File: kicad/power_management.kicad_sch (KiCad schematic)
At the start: 30 parts, among them J17 PJ-002AH, SW1 RESET, U1 TPS54302DDCR, U12 TPS3823-33DBVR, U2 AMS1117-3.3

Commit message: fix: Embed lib_symbols, fix invalid lib_ids, bump to KiCad 9 format
- Embed complete (lib_symbols) definitions in all 5 sub-sheets so symbols
  render as real parts instead of '??' placeholders (files now self-contained)
- Substitute invalid lib_ids with valid library symbols:
  Device:CP -> Device:C_Polarized, Diode:PESD3V3S2USF -> Diode:PESD3V3S1UL,
  Diode:PESD5V0S1BSF -> Diode:PESD5V0S1UL, Isolator:PC817X2 -> Isolator:PC817
- Bump file format version 20231120 -> 20250114 (removes 'older version' warning)
- Left-justify header text blocks so long lines stay within the A3 frame

Validated: kicad-cli SVG render (all real symbols, within frame), clean-room
eeschema GUI render with broken library table (no '??'), and kicad-cli ERC
runs without crashing (425 violations are expected unconnected-pin/dangling-
label items, resolved during per-sheet wiring).

Co-Authored-By: Devin AI <158243242+devin-ai-integration[bot]@users.noreply.github.com>
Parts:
- C10, C2: symbol Device:CP -> Device:C_Polarized
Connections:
- net 12V_FUSED: now also D2.2 (A), F1.2
- net 12V_RAIL: now also C1.1, C2.1, C3.1, C4.1, D2.1 (K), FB1.1, R_LED1.1, U1.3 (VIN), U1.5 (EN)
- net 3V3_RAIL: now also C10.1, C30.1, C9.1, R_LED3.1, R_WDI.2, U12.5 (VDD), U2.2 (VO)
- net 5V_RAIL: now also C5.1, C6.1, C8.1, L1.2, R1.1, R_LED2.1, U2.3 (VI)
- net FB: now also R1.2, R2.2, U1.4 (FB)
- net GND: now also C1.2, C10.2, C2.2, C3.2, C30.2, C4.2, C5.2, C6.2, C8.2, C9.2, D1.2 (A2), J17.2, LED1.2 (A), LED2.2 (A), LED3.2 (A), R2.1, SW1.1, U1.1 (GND), U12.2 (GND), U2.1 (GND)
- net MCU_NRST: now also U12.1 (~{RESET})
- net MCU_WDI: now also R_WDI.1, U12.4 (WDI)
- net VIN_12V: now also D1.1 (A1), F1.1, J17.1, J17.3
- new net: C7.1, C7.2, L1.1, U1.2 (SW), U1.6 (BOOT)
- new net: LED1.1 (K), R_LED1.2
- new net: LED2.1 (K), R_LED2.2
- new net: LED3.1 (K), R_LED3.2
- new net: SW1.2, U12.3 (~{MR})
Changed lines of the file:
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@@
 (kicad_sch
-  (version 20231120)
+  (version 20250114)
   (generator "devin")
   (generator_version "1.0")
@@
   )
   (symbol
-    (lib_id "Device:CP")
+    (lib_id "Device:C_Polarized")
     (at 93.98 55.88 0)
     (unit 1)
@@
   )
   (symbol
-    (lib_id "Device:CP")
+    (lib_id "Device:C_Polarized")
     (at 241.3 81.28 0)
     (unit 1)
@@
   (text "POWER MANAGEMENT BLOCK\n12V → 5V (Buck TPS54302) → 3.3V (LDO AMS1117)\nProtection: TVS + PTC + Schottky\nWatchdog: TPS3823 on all tiers"
     (at 25.4 25.4 0)
-    (effects (font (size 2.54 2.54)))
+    (effects (font (size 2.54 2.54)) (justify left))
     (uuid "txt-title")
   )

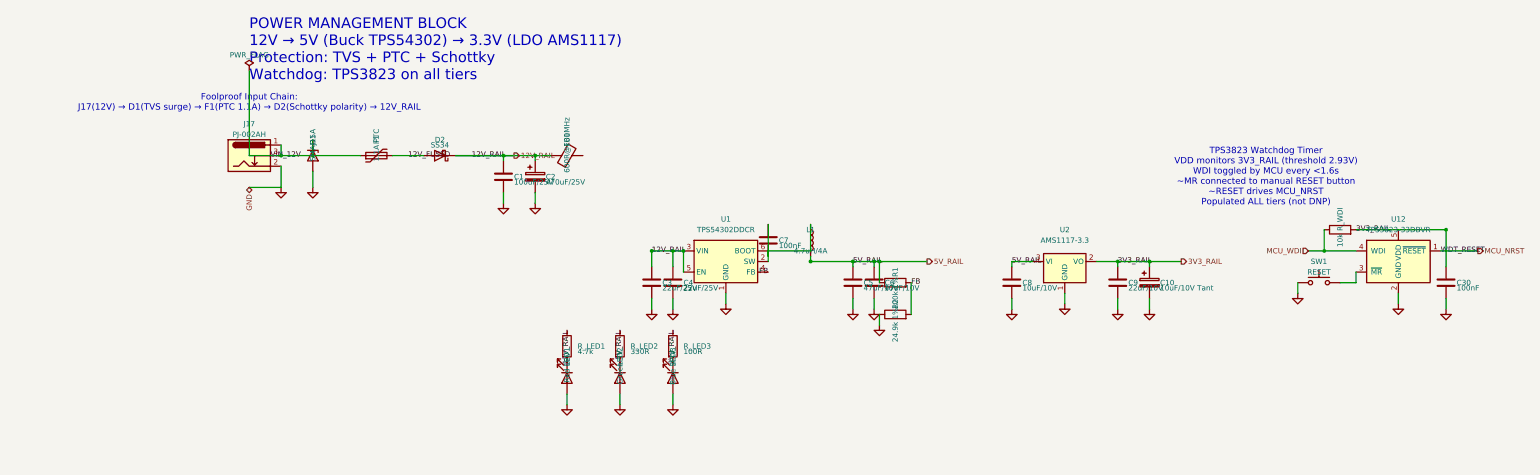
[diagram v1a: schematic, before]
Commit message: fix: Re-annotate components with unique global references + add instances blocks
Root cause: symbol instances lacked (instances ...) blocks, so KiCad treated
all references as unannotated/duplicated (108 duplicate_reference ERC errors)
and produced auto-renamed names (C_DO2, U3_2A, ...) on annotation.

Fix: assign globally-unique sequential standard references (R1..R28, C1..C27,
U1..U20, D1..D18, J1..J21, etc.) and embed a proper (instances) block per
symbol with the correct hierarchical path. Each MCP6002 kept as its own IC
(unit A) to preserve per-channel galvanic isolation (pH/ORP/DO).

ERC: duplicate_reference 108 -> 0, unannotated 1 -> 0.
Co-Authored-By: Devin AI <158243242+devin-ai-integration[bot]@users.noreply.github.com>
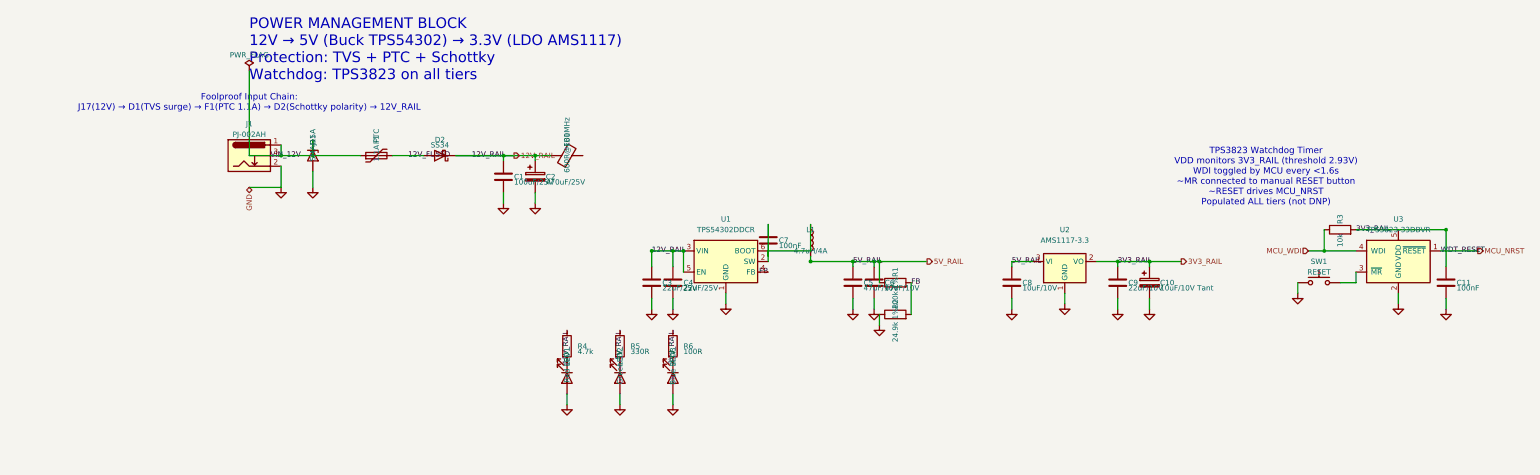
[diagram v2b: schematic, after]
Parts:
- renumbered C30 to C11, J17 to J1, R_WDI to R3, R_LED1 to R4, R_LED2 to R5, R_LED3 to R6, U12 to U3
